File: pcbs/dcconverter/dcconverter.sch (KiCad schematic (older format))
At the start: 41 parts, among them IC1 NCP7805TG, J1 190-9991, J3 146-8335, J4 766-6604, J5 766-6604, Q1 NGTB40N120FL2WG, Q10 TS13003CT, Q2 FQP47P06, Q3 2SK3747-1E, Q4 2SK3747-1E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

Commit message: Use correct footprint for D1
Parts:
- D1: footprint Diode_THT:D_DO-247_Vertical -> Custom:DSS60-0045B_Vertical
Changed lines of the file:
@@
 F 0 "D1" V 2854 2780 50  0000 L CNN
 F 1 "DSS60-0045B" V 2945 2780 50  0000 L CNN
-F 2 "Diode_THT:D_DO-247_Vertical" H 2900 2700 50  0001 C CNN
+F 2 "Custom:DSS60-0045B_Vertical" H 2900 2700 50  0001 C CNN
 F 3 "~" H 2900 2700 50  0001 C CNN
 	1    2900 2700

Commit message: Use correct footprint for NGTB40N120FL2WG
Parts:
- Q1: footprint Package_TO_SOT_THT:TO-247-3_Vertical -> Custom:NGTB40N120FL2WG_Vertical
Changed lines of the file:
@@
 F 0 "Q1" V 2778 2050 50  0000 C CNN
 F 1 "NGTB40N120FL2WG" V 2687 2050 50  0000 C CNN
-F 2 "Package_TO_SOT_THT:TO-247-3_Vertical" H 2650 2150 50  0001 C CNN
+F 2 "Custom:NGTB40N120FL2WG_Vertical" H 2650 2150 50  0001 C CNN
 F 3 "~" H 2450 2050 50  0001 C CNN
 	1    2450 2050

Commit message: Use correct footprint for Q2
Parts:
- Q2: footprint TO254P483X1016X2261-3P -> Custom:FQP47P06_Vertical_Wide
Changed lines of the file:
@@
 F 0 "Q2" V 9067 2350 50  0000 C CNN
 F 1 "FQP47P06" V 8976 2350 50  0000 C CNN
-F 2 "TO254P483X1016X2261-3P" H 8950 2200 50  0001 L CNN
+F 2 "Custom:FQP47P06_Vertical_Wide" H 8950 2200 50  0001 L CNN
 F 3 "http://uk.rs-online.com/web/p/products/6715127P" H 8950 2100 50  0001 L CNN
 F 4 "Trans MOSFET P-CH 60V 47A 3-Pin TO-220" H 8950 2000 50  0001 L CNN "Description"

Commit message: Use correct footprint for Q8
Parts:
- Q8: footprint Package_TO_SOT_THT:TO-220-3_Horizontal_TabDown -> Custom:FDP20N50_Horizontal_TabDown
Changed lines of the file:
@@
 F 0 "Q8" H 9404 5096 50  0000 L CNN
 F 1 "FDP20N50" H 9404 5005 50  0000 L CNN
-F 2 "Package_TO_SOT_THT:TO-220-3_Horizontal_TabDown" H 9400 4975 50  0001 L CIN
+F 2 "Custom:FDP20N50_Horizontal_TabDown" H 9400 4975 50  0001 L CIN
 F 3 "" H 9200 5050 50  0001 L CNN
 	1    9200 5050

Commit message: Use correct footprint for Q7
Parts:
- Q7: footprint Package_TO_SOT_THT:TO-220-3_Horizontal_TabDown -> Custom:FQP3P50_Horizontal_TabDown
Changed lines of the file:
@@
 F 0 "Q7" H 9405 4104 50  0000 L CNN
 F 1 "FQP3P50" H 9405 4195 50  0000 L CNN
-F 2 "Package_TO_SOT_THT:TO-220-3_Horizontal_TabDown" H 9400 4075 50  0001 L CIN
+F 2 "Custom:FQP3P50_Horizontal_TabDown" H 9400 4075 50  0001 L CIN
 F 3 "" H 9200 4150 50  0001 L CNN
 	1    9200 4150

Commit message: Use correct footprint for Q3 and Q4
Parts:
- Q3, Q4: footprint Package_TO_SOT_THT:TO-3P-3_Horizontal_TabDown -> Custom:2SK3747_TabDown
- Q5, Q6: footprint Package_TO_SOT_THT:TO-92_Inline -> Custom:TS13003CT_wide
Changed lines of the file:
@@
 F 0 "Q3" H 2804 4696 50  0000 L CNN
 F 1 "2SK3747-1E" H 2804 4605 50  0000 L CNN
-F 2 "Package_TO_SOT_THT:TO-3P-3_Horizontal_TabDown" H 2800 4575 50  0001 L CIN
+F 2 "Custom:2SK3747_TabDown" H 2800 4575 50  0001 L CIN
 F 3 "https://www.onsemi.com/pub/Collateral/NDS7002A-D.PDF" H 2600 4650 50  0001 L CNN
 	1    2600 4650
@@
 F 0 "Q4" H 6354 4696 50  0000 L CNN
 F 1 "2SK3747-1E" H 6354 4605 50  0000 L CNN
-F 2 "Package_TO_SOT_THT:TO-3P-3_Horizontal_TabDown" H 6350 4575 50  0001 L CIN
+F 2 "Custom:2SK3747_TabDown" H 6350 4575 50  0001 L CIN
 F 3 "https://www.onsemi.com/pub/Collateral/NDS7002A-D.PDF" H 6150 4650 50  0001 L CNN
 	1    6150 4650
@@
 F 0 "Q5" H 7940 4646 50  0000 L CNN
 F 1 "TS13003CT" H 7940 4555 50  0000 L CNN
-F 2 "Package_TO_SOT_THT:TO-92_Inline" H 7950 4525 50  0001 L CIN
+F 2 "Custom:TS13003CT_wide" H 7950 4525 50  0001 L CIN
 F 3 "" H 7750 4600 50  0001 L CNN
 	1    7750 4600
@@
 F 0 "Q6" H 7940 5196 50  0000 L CNN
 F 1 "TS13003CT" H 7940 5105 50  0000 L CNN
-F 2 "Package_TO_SOT_THT:TO-92_Inline" H 7950 5075 50  0001 L CIN
+F 2 "Custom:TS13003CT_wide" H 7950 5075 50  0001 L CIN
 F 3 "" H 7750 5150 50  0001 L CNN
 	1    7750 5150

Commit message: Use the windings in parallel
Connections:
- net at D1.1 (K), L1.1 (L1_1), Q1.2 (E): now also L1.2 (L2_1)
- net at L1.3 (L1_2): now also C1.1, L1.4 (L2_2), Q2.3, R1.1; no longer L1.2 (L2_1)
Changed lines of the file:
@@
 	1    0    0    -1
 $EndComp
-Wire Wire Line
-	2900 1950 3550 1950
-Connection ~ 2900 1950
 $Comp
 L Custom:CP-Device C1
@@
 Wire Wire Line
 	3800 5350 3700 5350
-Wire Wire Line
-	4650 1950 4650 2450
-Wire Wire Line
-	4650 2450 3400 2450
-Wire Wire Line
-	3400 2450 3400 2200
-Wire Wire Line
-	3400 2200 3550 2200
-Wire Wire Line
-	4500 1950 4650 1950
-Wire Wire Line
-	4750 2200 4750 1950
-Wire Wire Line
-	4750 1950 5050 1950
-Wire Wire Line
-	4500 2200 4750 2200
 Connection ~ 5050 1950
 $Comp
@@
 	6600 5000 6400 5000
 Connection ~ 6400 5000
+Wire Wire Line
+	2900 1950 3350 1950
+Connection ~ 2900 1950
+Wire Wire Line
+	3550 2200 3350 2200
+Wire Wire Line
+	3350 2200 3350 1950
+Connection ~ 3350 1950
+Wire Wire Line
+	3350 1950 3550 1950
+Wire Wire Line
+	4500 1950 4650 1950
+Wire Wire Line
+	4500 2200 4650 2200
+Wire Wire Line
+	4650 2200 4650 1950
+Connection ~ 4650 1950
+Wire Wire Line
+	4650 1950 5050 1950
 $EndSCHEMATC

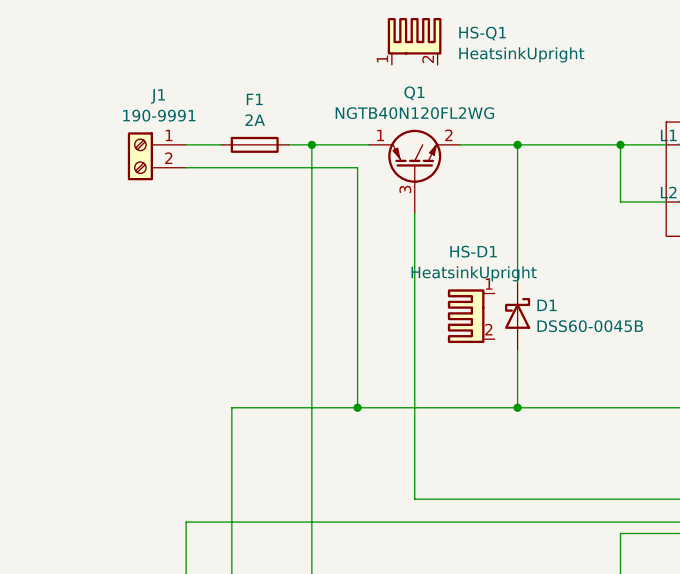
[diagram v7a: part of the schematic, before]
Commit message: Add reverse polarity protection
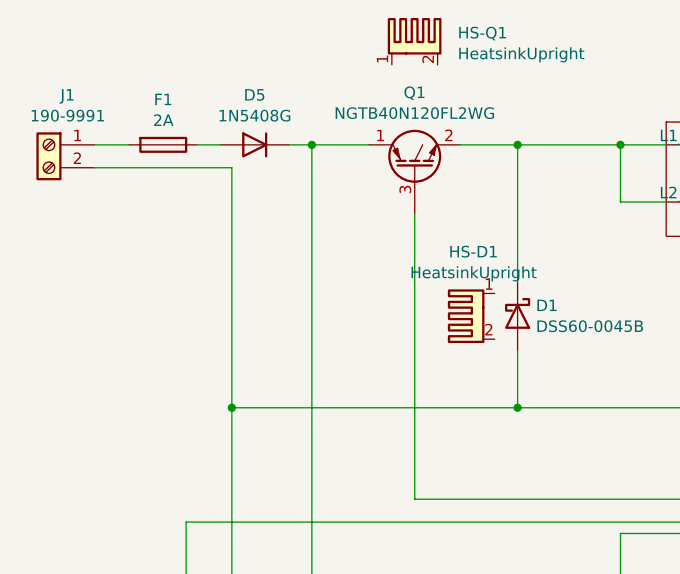
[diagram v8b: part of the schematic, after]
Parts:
- added D5: 1N5408G, Diode_THT:D_5W_P12.70mm_Horizontal, symbol Device:D
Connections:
- net at Q1.1 (C), Q3.3 (D), Q4.3 (D)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: now also D5.1 (K); no longer F1.1
- new net: D5.2 (A), F1.1
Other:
- moved on the sheet: F1, J1
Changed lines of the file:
@@
 L Connector:Screw_Terminal_01x02 J1
 U 1 1 5F938BEF
-P 1250 1950
-F 0 "J1" H 1168 2167 50  0000 C CNN
-F 1 "190-9991" H 1168 2076 50  0000 C CNN
-F 2 "Custom:TerminalBlock_2pin_10mm" H 1250 1950 50  0001 C CNN
-F 3 "~" H 1250 1950 50  0001 C CNN
-	1    1250 1950
+P 850 1950
+F 0 "J1" H 768 2167 50  0000 C CNN
+F 1 "190-9991" H 768 2076 50  0000 C CNN
+F 2 "Custom:TerminalBlock_2pin_10mm" H 850 1950 50  0001 C CNN
+F 3 "~" H 850 1950 50  0001 C CNN
+	1    850  1950
 	-1   0    0    -1
 $EndComp
@@
 L Device:Fuse F1
 U 1 1 5F93C935
-P 1750 1950
-F 0 "F1" V 1553 1950 50  0000 C CNN
-F 1 "2A" V 1644 1950 50  0000 C CNN
-F 2 "Fuse:Fuseholder_Cylinder-5x20mm_Schurter_0031_8201_Horizontal_Open" V 1680 1950 50  0001 C CNN
-F 3 "~" H 1750 1950 50  0001 C CNN
-	1    1750 1950
-	0    1    1    0
-$EndComp
-Wire Wire Line
-	1450 1950 1600 1950
-Wire Wire Line
-	1900 1950 2000 1950
+P 1350 1950
+F 0 "F1" V 1153 1950 50  0000 C CNN
+F 1 "2A" V 1244 1950 50  0000 C CNN
+F 2 "Fuse:Fuseholder_Cylinder-5x20mm_Schurter_0031_8201_Horizontal_Open" V 1280 1950 50  0001 C CNN
+F 3 "~" H 1350 1950 50  0001 C CNN
+	1    1350 1950
+	0    1    1    0
+$EndComp
+Wire Wire Line
+	1050 1950 1200 1950
 $Comp
 L Device:D_Schottky D1
@@
 	2900 3100 2900 2850
 Wire Wire Line
-	1450 2050 2200 2050
-Wire Wire Line
-	2200 2050 2200 3100
+	1050 2050 1650 2050
 Connection ~ 2900 3100
 $Comp
@@
 	9950 2050 9950 3100
 Wire Wire Line
-	2200 3100 2900 3100
-Connection ~ 2200 3100
-Wire Wire Line
 	5550 2500 5750 2500
 $Comp
@@
 Wire Wire Line
 	1800 4000 1800 4100
-Connection ~ 2000 1950
 Wire Wire Line
 	2000 1950 2250 1950
@@
 Wire Wire Line
 	1800 5750 1650 5750
-Wire Wire Line
-	1650 3100 2200 3100
 Connection ~ 1800 5750
 $Comp
@@
 Wire Wire Line
 	4650 1950 5050 1950
+$Comp
+L Device:D D5
+U 1 1 5FBA5BAB
+P 1750 1950
+F 0 "D5" H 1750 2167 50  0000 C CNN
+F 1 "1N5408G" H 1750 2076 50  0000 C CNN
+F 2 "Diode_THT:D_5W_P12.70mm_Horizontal" H 1750 1950 50  0001 C CNN
+F 3 "~" H 1750 1950 50  0001 C CNN
+	1    1750 1950
+	-1   0    0    -1
+$EndComp
+Wire Wire Line
+	1500 1950 1600 1950
+Wire Wire Line
+	1900 1950 2000 1950
+Connection ~ 2000 1950
+Wire Wire Line
+	1650 3100 1650 2050
+Connection ~ 1650 3100
+Wire Wire Line
+	1650 3100 2900 3100
 $EndSCHEMATC
